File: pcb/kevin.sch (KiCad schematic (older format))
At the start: 83 parts, among them J1 battery, J2 joystick_analogic, J3 eink, J4 to-trackball-side, J5 trackball-side, SW00 SW_Push, SW01 SW_Push, SW02 SW_Push, SW03 SW_Push, SW04 SW_Push, SW05 SW_Push, SW10 SW_Push, SW11 SW_Push, SW12 SW_Push, SW13 SW_Push, SW14 SW_Push, SW15 SW_Push, SW20 SW_Push, SW21 SW_Push, SW22 SW_Push, SW23 SW_Push, SW24 SW_Push, SW25 SW_Push, SW32 SW_Push, SW33 SW_Push, SW34 SW_Push, SW35 SW_Push, U1 nice_nano, U2 XC6206P202MR-G, U3 PMW3360DM-T2QU

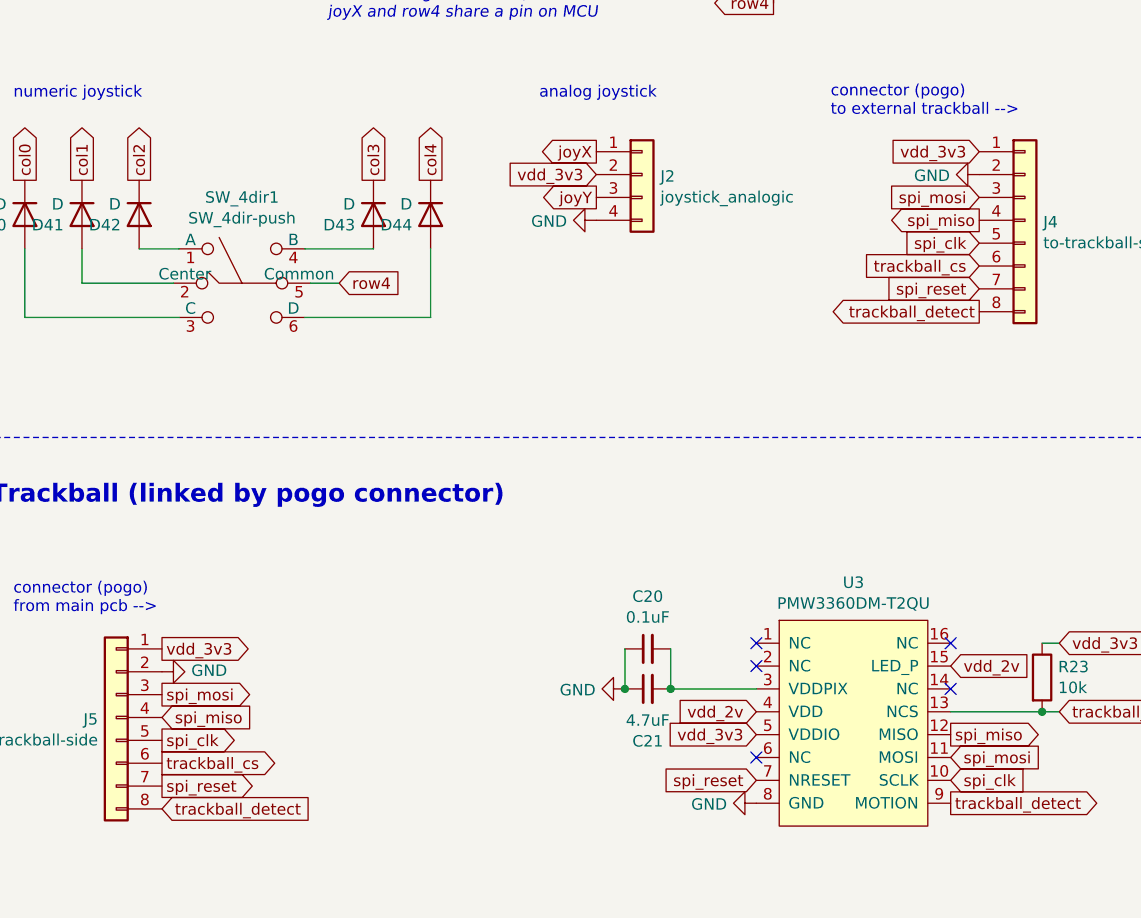
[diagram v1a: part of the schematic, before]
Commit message: Adding 3D view of components Correction on mill-max size (mills/mm) Changing resistor to 0805 (like capacitors) Separation of GND and VCC on mill-max connectors to avoid shortcuts
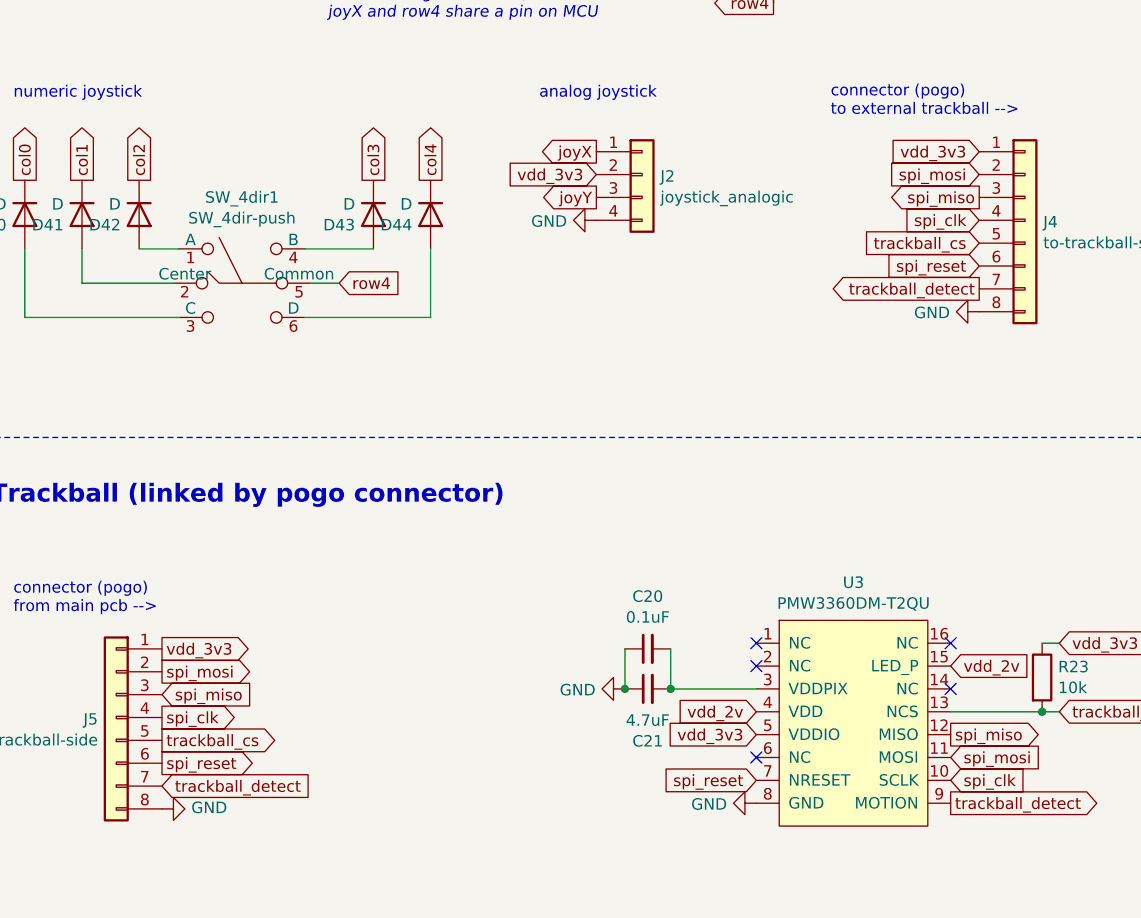
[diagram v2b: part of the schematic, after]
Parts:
- R02: footprint kevin:R_1206_reversible -> kevin:R_0805_reversible
- R23: footprint Resistor_SMD:R_1206_3216Metric_Pad1.30x1.75mm_HandSolder -> Resistor_SMD:R_0805_2012Metric_Pad1.20x1.40mm_HandSolder
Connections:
- net GND: now also J4.8 (Pin_8), J5.8 (Pin_8); no longer J4.2 (Pin_2), J5.2 (Pin_2)
- net spi_clk: now also J4.4 (Pin_4), J5.4 (Pin_4); no longer J4.5 (Pin_5), J5.5 (Pin_5)
- net spi_miso: now also J4.3 (Pin_3), J5.3 (Pin_3); no longer J4.4 (Pin_4), J5.4 (Pin_4)
- net spi_mosi: now also J4.2 (Pin_2), J5.2 (Pin_2); no longer J4.3 (Pin_3), J5.3 (Pin_3)
- net spi_reset: now also J4.6 (Pin_6), J5.6 (Pin_6); no longer J4.7 (Pin_7), J5.7 (Pin_7)
- net trackball_cs: now also J4.5 (Pin_5), J5.5 (Pin_5); no longer J4.6 (Pin_6), J5.6 (Pin_6)
- net trackball_detect: now also J4.7 (Pin_7), J5.7 (Pin_7); no longer J4.8 (Pin_8), J5.8 (Pin_8)
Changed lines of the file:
@@
 Comment4 "Half part of split keyboard"
 $EndDescr
-Text GLabel 4950 5225 0    50   Output ~ 0
-trackball_detect
-Text GLabel 4950 5125 0    50   Input ~ 0
-spi_reset
 Text Notes 4300 4375 0    50   ~ 0
 connector (pogo)\nto external trackball -->
-Text GLabel 4950 5025 0    50   Input ~ 0
-trackball_cs
-Text GLabel 4950 4825 0    50   Output ~ 0
-spi_miso
-Text GLabel 4950 4925 0    50   Input ~ 0
-spi_clk
-Text GLabel 4950 4725 0    50   Input ~ 0
-spi_mosi
 $Comp
 L power:GND #PWR0115
 U 1 1 61108E9E
-P 4950 4625
-F 0 "#PWR0115" H 4950 4375 50  0001 C CNN
-F 1 "GND" V 4955 4497 50  0000 R CNN
-F 2 "" H 4950 4625 50  0001 C CNN
-F 3 "" H 4950 4625 50  0001 C CNN
-	1    4950 4625
+P 4950 5225
+F 0 "#PWR0115" H 4950 4975 50  0001 C CNN
+F 1 "GND" V 4955 5097 50  0000 R CNN
+F 2 "" H 4950 5225 50  0001 C CNN
+F 3 "" H 4950 5225 50  0001 C CNN
+	1    4950 5225
 	0    1    1    0
 $EndComp
@@
 L power:GND #PWR0116
 U 1 1 626EE7E6
-P 1375 6800
-F 0 "#PWR0116" H 1375 6550 50  0001 C CNN
-F 1 "GND" V 1380 6672 50  0000 R CNN
-F 2 "" H 1375 6800 50  0001 C CNN
-F 3 "" H 1375 6800 50  0001 C CNN
-	1    1375 6800
+P 1375 7400
+F 0 "#PWR0116" H 1375 7150 50  0001 C CNN
+F 1 "GND" V 1380 7272 50  0000 R CNN
+F 2 "" H 1375 7400 50  0001 C CNN
+F 3 "" H 1375 7400 50  0001 C CNN
+	1    1375 7400
 	0    -1   -1   0
 $EndComp
-Text GLabel 1375 6900 2    50   Output ~ 0
+Text GLabel 1375 6800 2    50   Output ~ 0
 spi_mosi
-Text GLabel 1375 7000 2    50   Input ~ 0
+Text GLabel 1375 6900 2    50   Input ~ 0
 spi_miso
+Text GLabel 1375 7000 2    50   Output ~ 0
+spi_clk
 Text GLabel 1375 7100 2    50   Output ~ 0
-spi_clk
+trackball_cs
 Text GLabel 1375 7200 2    50   Output ~ 0
-trackball_cs
-Text GLabel 1375 7300 2    50   Output ~ 0
 spi_reset
-Text GLabel 1375 7400 2    50   Input ~ 0
+Text GLabel 1375 7300 2    50   Input ~ 0
 trackball_detect
 Text GLabel 5300 6675 2    50   Input ~ 0
@@
 F 0 "R02" H 10270 1621 50  0000 L CNN
 F 1 "10k" H 10270 1530 50  0000 L CNN
-F 2 "kevin:R_1206_reversible" V 10130 1575 50  0001 C CNN
+F 2 "kevin:R_0805_reversible" V 10130 1575 50  0001 C CNN
 F 3 "~" H 10200 1575 50  0001 C CNN
 	1    10200 1575
@@
 F 0 "R23" H 5295 6871 50  0000 L CNN
 F 1 "10k" H 5295 6780 50  0000 L CNN
-F 2 "Resistor_SMD:R_1206_3216Metric_Pad1.30x1.75mm_HandSolder" V 5155 6825 50  0001 C CNN
+F 2 "Resistor_SMD:R_0805_2012Metric_Pad1.20x1.40mm_HandSolder" V 5155 6825 50  0001 C CNN
 F 3 "~" H 5225 6825 50  0001 C CNN
 	1    5225 6825
@@
 Wire Notes Line style solid
 	8700 6525 8700 475
+Text GLabel 4950 4625 0    50   Input ~ 0
+spi_mosi
+Text GLabel 4950 4825 0    50   Input ~ 0
+spi_clk
+Text GLabel 4950 4725 0    50   Output ~ 0
+spi_miso
+Text GLabel 4950 4925 0    50   Input ~ 0
+trackball_cs
+Text GLabel 4950 5025 0    50   Input ~ 0
+spi_reset
+Text GLabel 4950 5125 0    50   Output ~ 0
+trackball_detect
 $EndSCHEMATC
